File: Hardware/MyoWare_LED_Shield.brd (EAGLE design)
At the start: 52.1 x 21.6 mm, 20 parts, among them IC1 LM3914V

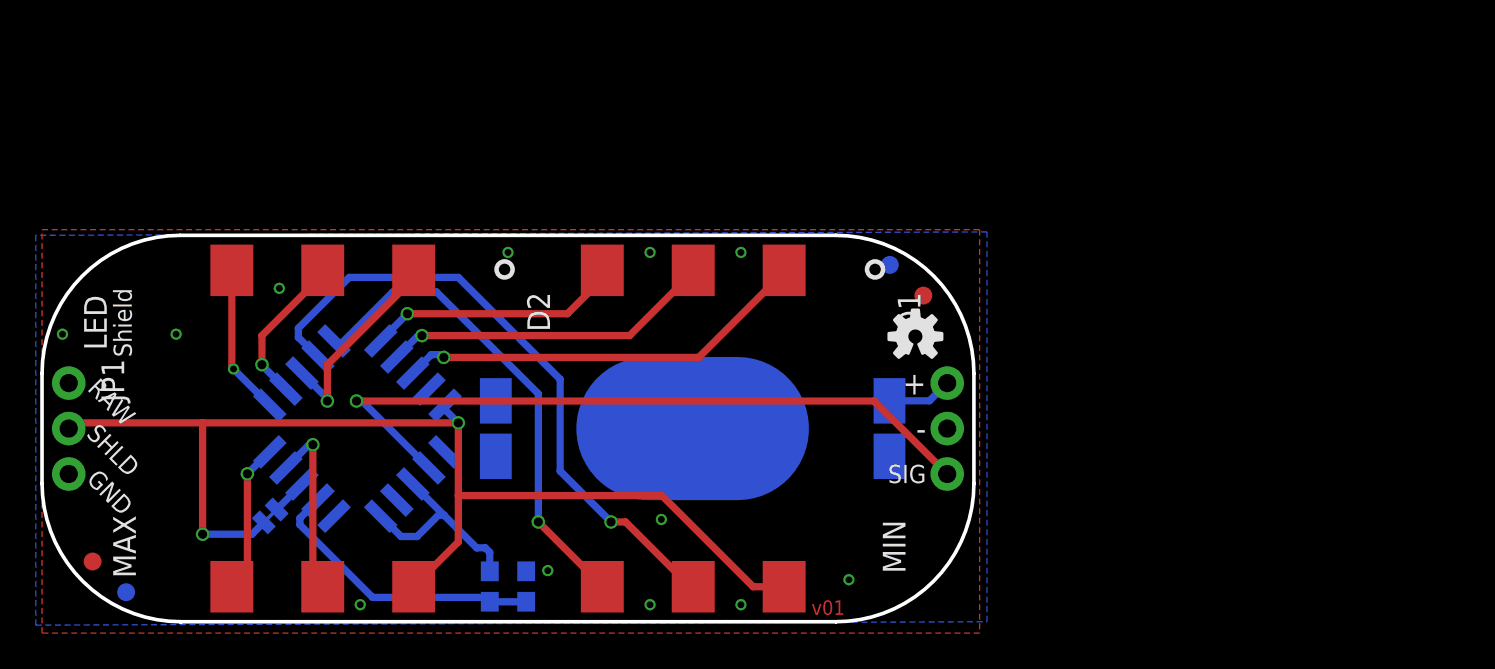
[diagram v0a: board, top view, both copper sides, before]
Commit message: Started move to LiPo based design
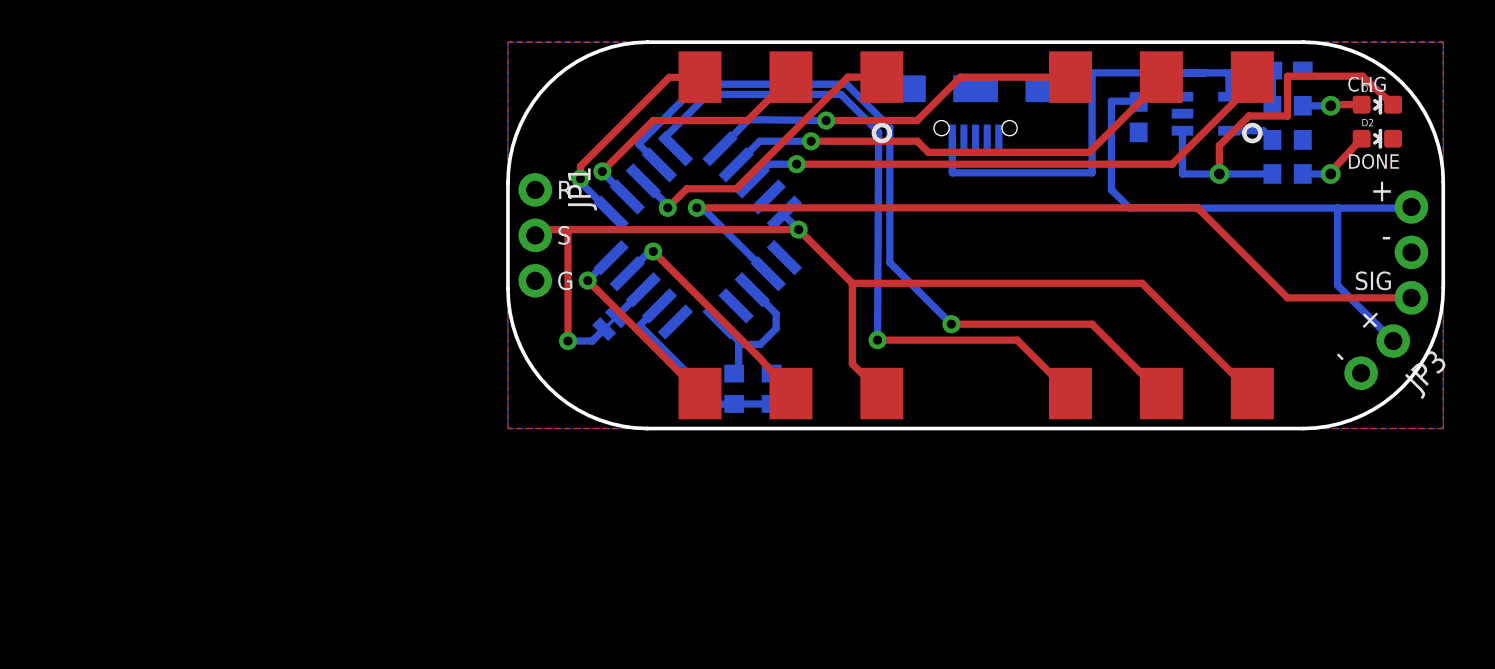
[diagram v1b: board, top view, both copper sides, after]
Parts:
- removed BAT1: 20mm coincell, SparkFun-Electromechanical:BATTCON_20MM_4LEGS
- removed FID1, FID2, FID3, FID4: FIDUCIAL1X2, SparkFun-Aesthetics:FIDUCIAL-1X2
- removed LOGO1: SFE_LOGO_NAME_FLAME.1_INCH, SparkFun-Aesthetics:SFE_LOGO_NAME_FLAME_.1
- removed LOGO2: OSHW-LOGOS, SparkFun-Aesthetics:OSHW-LOGO-S
- removed U$3: (no value), advancer-technologies:ROHS
- removed U$5: (no value), advancer-technologies:PB-FREE
- added C1, C2: 4.7uF, SparkFun-Capacitors:0603-CAP
- added JP3: (no value), SparkFun-Connectors:1X02_NO_SILK
- added JP4: (no value), SparkFun-Connectors:USB-B-MICRO-SMD_V03
- added R3, R5: 330, resistor:R0603
- added R4: 10k, resistor:R0603
- added U$1, U$2: SMA-B500, advancer-technologies:LED_BAR_SMD
- added U1: MCP73831, SparkFun-PowerIC:SOT23-5
- D1, D2: value SMA-B500 -> RED; device Testing:LED_BAR_SMD -> SparkFun-LED:LED-0603
- IC1: device Testing:PLCC20S -> national-semiconductor:PLCC20S
- R1: value 10K -> 6.49k; device SparkFun-Resistors:0603-RES -> resistor:R0603
- R2: value 8K2 -> 7.5k; device SparkFun-Resistors:0603-RES -> resistor:R0603
- SJ1: value JUMPER-PAD-2-NC_BY_TRACE -> SOLDERJUMPERTRACE; device SparkFun-Passives:PAD-JUMPER-2-NC_BY_TRACE_YES_SILK -> SparkFun:SJ_2S-TRACE
- moved D2 61.1 mm to (48.6, 16.2), turned to 270 degrees
- moved D1 42.3 mm to (48.6, 18.1), turned to 270 degrees
- moved U$6 34.0 mm to (26.1, 2.22)
- moved JP1 28.2 mm to (1.52, 13.3)
- moved JP2 27.7 mm to (50.5, 12.4)
- moved FRAME1 27.7 mm to (-12.2, -11.7)
- moved U$9 24.3 mm to (4.89, 17.6)
- moved IC1 21.9 mm to (10.6, 10.8)
- moved SJ1 21.9 mm to (5.73, 5.91)
- moved R2 17.6 mm to (14.7, 2.22)
- moved R1 17.6 mm to (12.6, 2.22)
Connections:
- removed net VCC: BAT1.1, JP2.1
- new net +VS: C2.1, JP2.1, JP3.1, U1.3
- new net N$10: D1.A, R3.1
- new net N$15: D1.C, R5.1, U1.1
- new net N$17: R4.2, U1.5
- new net N$7: C1.1, JP4.VBUS1, R3.2, U1.4
- new net N$9: D2.A, R5.2
- net GND: now also C1.2, C2.2, D2.C, JP3.2, JP4.GND1, R4.1, U1.2; no longer BAT1.2
- net N$1: now also U$1.1; no longer D1.1
- net N$11: now also U$2.2; no longer D2.2
- net N$12: now also U$2.3; no longer D2.3
- net N$13: now also U$2.4; no longer D2.4
- net N$14: now also U$2.5; no longer D2.5
- net N$2: now also U$1.2; no longer D1.2
- net N$3: now also U$1.5; no longer D1.5
- net N$4: now also U$1.3; no longer D1.3
- net N$5: now also U$2.1; no longer D2.1
- net N$8: now also U$1.4; no longer D1.4
- net SHLD_PWR: now also U$1.6, U$2.6; no longer D1.6, D2.6
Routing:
- net +VS: track 0.00 -> 35.2 mm
- net N$7: track 0.00 -> 30.1 mm
- net N$15: track 0.00 -> 22.3 mm, vias 0 -> 1
- net N$8: track 27.3 -> 38.3 mm
- net N$3: track 35.7 -> 44.1 mm
- net N$2: track 18.6 -> 26.4 mm
- net N$1: track 23.3 -> 30.6 mm
- net SIG: track 40.3 -> 47.5 mm
- net N$4: track 14.3 -> 21.3 mm
- net N$11: track 8.60 -> 14.7 mm
- net N$5: track 11.5 -> 17.1 mm
- net N$19: track 16.2 -> 10.7 mm
- net N$9: track 0.00 -> 4.21 mm, vias 0 -> 1
- net VCC: track 3.63 -> 0.00 mm
- net N$12: track 8.55 -> 12.1 mm
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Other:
- board size 52.1 x 21.6 mm -> 52.3 x 21.6 mm
- board text added: "BATTERY GOES HERE"
- board text added: "CHG"
- board text added: "DONE"
- board text added: "G"
- board text added: "R"
- board text added: "S"
- board text removed: "All units in inches"
- board text removed: "GND"
- board text removed: "LED"
- board text removed: "MAX"
- board text removed: "MIN"
- board text removed: "RAW"
- board text removed: "SHLD"
- board text removed: "Shield"
- board text removed: "v01"

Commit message: Design rules checked
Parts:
- removed IC1: LM3914V, national-semiconductor:PLCC20S
- removed SJ1: SOLDERJUMPERTRACE, SparkFun:SJ_2S-TRACE
- removed U$1, U$2: SMA-B500, advancer-technologies:LED_BAR_SMD
- added D3, D4: SMA-B500, Testing:LED_BAR_SMD
- added FID1, FID2, FID3, FID4: FIDUCIAL1X2, SparkFun-Aesthetics:FIDUCIAL-1X2
- added LOGO1: SFE_LOGO_FLAME.1_INCH, SparkFun-Aesthetics:SFE_LOGO_FLAME_.1
- added LOGO2: OSHW-LOGOS, SparkFun-Aesthetics:OSHW-LOGO-S
- added MODE: JUMPER-PAD-2-NC_BY_TRACE, SparkFun-Passives:PAD-JUMPER-2-NC_BY_TRACE_YES_SILK
- added U2: LM3914V, Testing:PLCC20S
- JP2: value Power -> Signal
- JP3: value (none) -> LiPo
- R3, R5: device resistor:R0603 -> SparkFun-Resistors:0603-RES
- R4: value 10k -> 10K; device resistor:R0603 -> SparkFun-Resistors:0603-RES
- moved JP2 1.08 mm to (50.5, 13.5)
- moved D2 0.13 mm to (48.6, 16.3)
- moved R3 0.13 mm to (43.6, 18.2)
- moved R5 0.13 mm to (43.6, 14.4)
- moved JP3 0.13 mm to (49.5, 5.02)
- moved R1 0.13 mm to (12.6, 2.35)
- moved R2 0.13 mm to (14.7, 2.35)
- moved U$6 0.13 mm to (26.1, 2.35)
- moved C1 0.13 mm to (43.6, 20.1)
- moved C2 0.13 mm to (35.2, 17.5)
- moved D1 0.13 mm to (48.6, 18.2)
- moved JP1 0.13 mm to (1.52, 13.5)
- moved JP4 0.13 mm to (26.1, 19.1)
- moved R4 0.13 mm to (43.6, 16.3)
- moved U$9 0.13 mm to (4.89, 17.7)
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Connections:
- net N$7 renamed VBUS
- net GND: now also U2.2, U2.4; no longer IC1.2, IC1.4
- net N$1: now also D3.1, U2.1; no longer IC1.1, U$1.1
- net N$11: now also D4.2, U2.15; no longer IC1.15, U$2.2
- net N$12: now also D4.3, U2.14; no longer IC1.14, U$2.3
- net N$13: now also D4.4, U2.13; no longer IC1.13, U$2.4
- net N$14: now also D4.5, U2.12; no longer IC1.12, U$2.5
- net N$19: now also U2.10; no longer IC1.10
- net N$2: now also D3.2, U2.20; no longer IC1.20, U$1.2
- net N$20: now also U2.6, U2.8; no longer IC1.6, IC1.8
- net N$3: now also D3.5, U2.17; no longer IC1.17, U$1.5
- net N$4: now also D3.3, U2.19; no longer IC1.19, U$1.3
- net N$5: now also D4.1, U2.16; no longer IC1.16, U$2.1
- net N$6: now also MODE.1, U2.11; no longer IC1.11, SJ1.1
- net N$8: now also D3.4, U2.18; no longer IC1.18, U$1.4
- net SHLD_PWR: now also D3.6, D4.6, MODE.2, U2.3; no longer IC1.3, SJ1.2, U$1.6, U$2.6
- net SIG: now also U2.5; no longer IC1.5
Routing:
- net +VS: track 35.2 -> 36.1 mm
- net N$3: track 44.1 -> 43.6 mm
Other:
- board size 52.3 x 21.6 mm -> 52.3 x 21.8 mm
- board text added: "ALL UNITS IN INCHES"
- board text added: "LED SHIELD"
- board text added: "MODE"
- board text added: "v02"

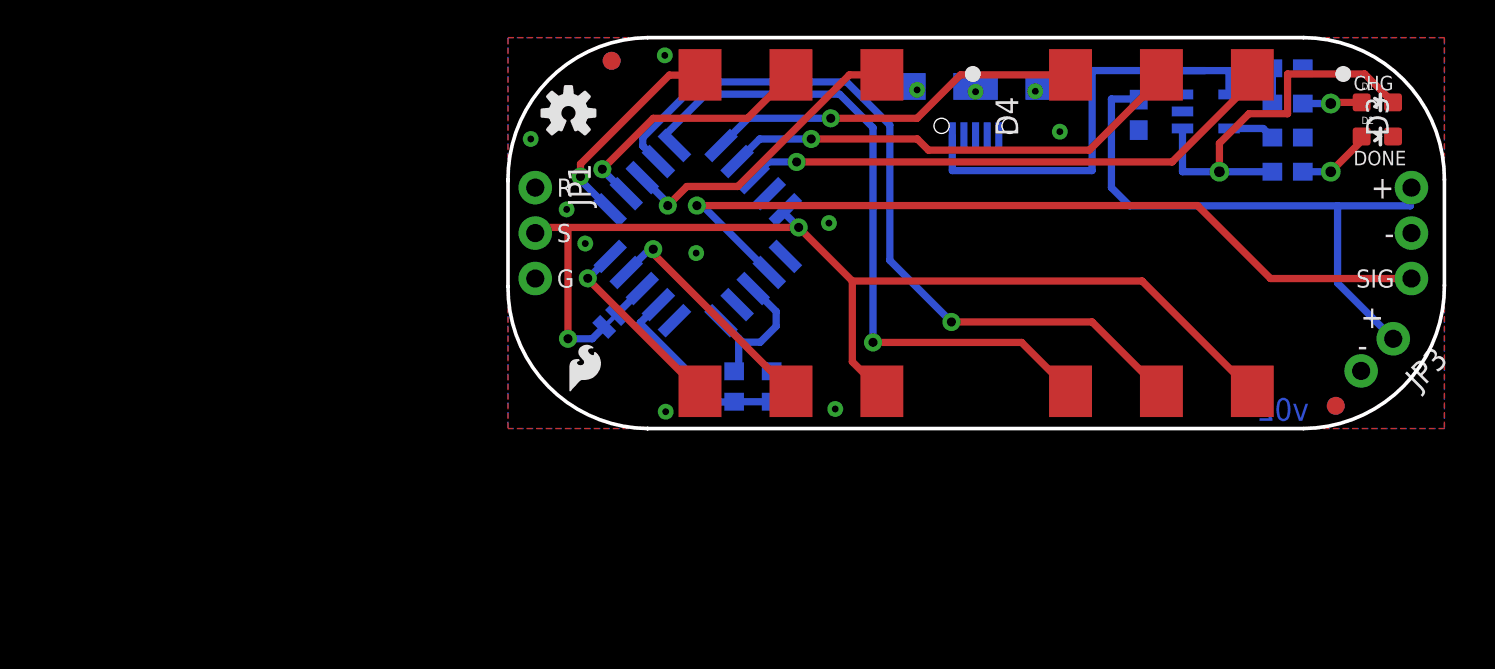
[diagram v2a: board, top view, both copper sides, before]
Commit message: Tweaks (mostly silk and info)
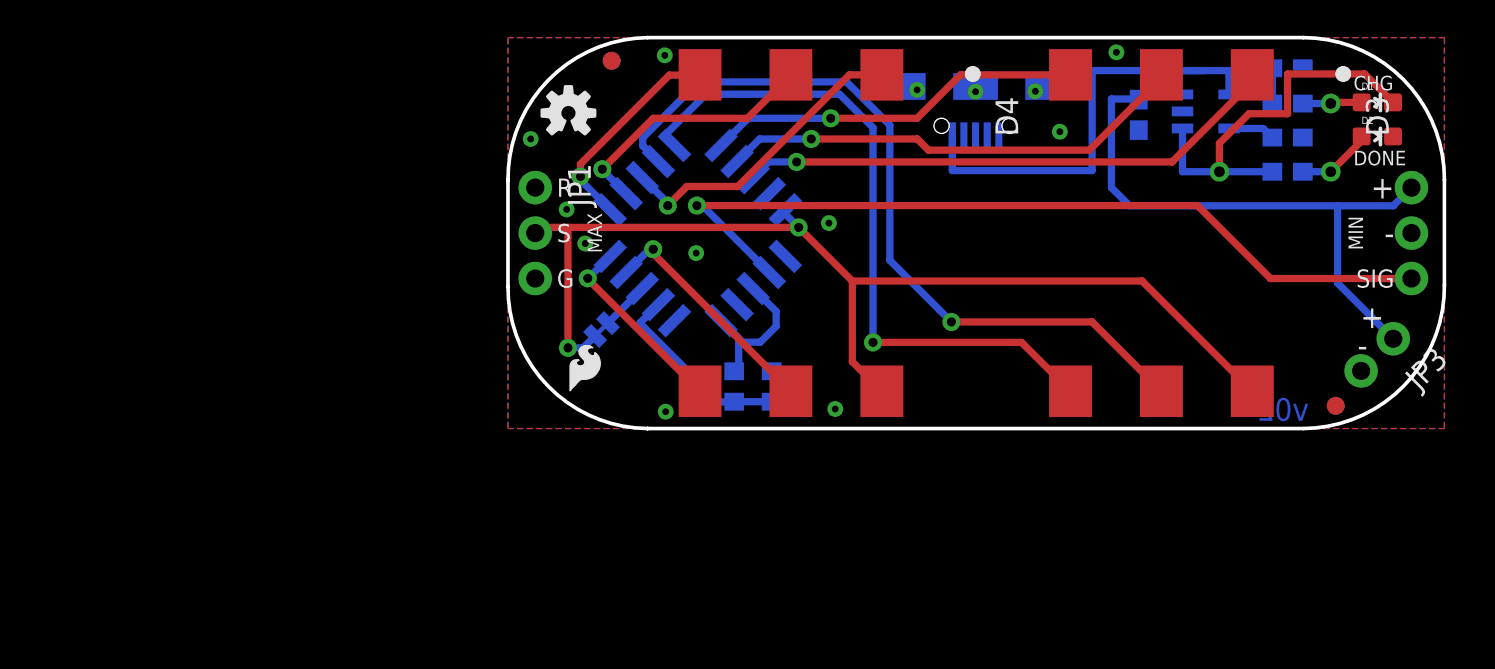
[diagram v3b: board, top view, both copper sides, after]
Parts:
- moved MODE 0.72 mm to (5.23, 5.53)
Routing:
- net N$6: track 2.01 -> 2.73 mm
- net +VS: track 36.1 -> 35.6 mm
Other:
- board text added: "MAX"
- board text added: "MIN"
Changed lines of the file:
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@@
 <setting verticaltext="up"/>
 </settings>
-<grid distance="0.01" unitdist="inch" unit="inch" style="lines" multiple="1" display="yes" altdistance="1.96850394" altunitdist="mil" altunit="mil"/>
+<grid distance="0.02" unitdist="inch" unit="inch" style="lines" multiple="1" display="yes" altdistance="1.96850394" altunitdist="mil" altunit="mil"/>
 <layers>
 <layer number="1" name="Top" color="4" fill="1" visible="yes" active="yes"/>
@@
 <text x="48.70835" y="5.774646875" size="1.27" layer="22" ratio="20" rot="R135" align="center-left">+</text>
 <text x="46.82195" y="4.041546875" size="1.27" layer="22" ratio="17" rot="R135" align="center-left">-</text>
-<text x="47.244" y="19.304" size="0.8128" layer="21" ratio="17" align="center-left">CHG</text>
-<text x="47.244" y="15.113" size="0.8128" layer="21" ratio="17" align="center-left">DONE</text>
+<text x="47.244" y="19.304" size="0.8128" layer="21" font="vector" ratio="17" align="center-left">CHG</text>
+<text x="47.244" y="15.113" size="0.8128" layer="21" font="vector" ratio="17" align="center-left">DONE</text>
 <text x="18.288" y="-11.684" size="1.778" layer="51" font="vector">Brian E Kaminski of Advancer Technologies</text>
 <text x="-0.762" y="-14.478" size="1.778" layer="51" font="vector">Revised by: Brent Wilkins</text>
@@
 <text x="49.38" y="8.382" size="1.016" layer="22" ratio="17" rot="MR180" align="center-right">SIG</text>
 <text x="49.276" y="10.922" size="1.27" layer="22" ratio="17" rot="MR180" align="center-right">-</text>
-<text x="4.98475" y="3.6322" size="1.27" layer="22" font="vector" ratio="15" rot="MR180" align="center">MODE</text>
+<text x="5.49275" y="2.6162" size="1.27" layer="22" font="vector" ratio="15" rot="MR180" align="center">MODE</text>
 <text x="26.5176" y="22.9108" size="1.016" layer="47" font="vector" ratio="17" align="bottom-center">ALL UNITS IN INCHES</text>
 <text x="15.5956" y="20.2946" size="0.8128" layer="22" font="vector" ratio="17" rot="MR0" align="bottom-center">LED SHIELD</text>
 <dimension x1="0" y1="7.9375" x2="52.324" y2="8.001" x3="26.162" y3="-2.266596875" textsize="1.016" textratio="17" layer="47" dtype="horizontal" unit="inch"/>
 <dimension x1="7.8105" y1="0" x2="7.8105" y2="21.844" x3="-1.6764" y3="10.922" textsize="1.016" textratio="17" layer="47" unit="inch"/>
+<text x="4.849" y="10.922" size="0.8128" layer="21" font="vector" ratio="17" rot="R90" align="center">MAX</text>
+<text x="47.371" y="10.922" size="0.8128" layer="21" font="vector" ratio="17" rot="R90" align="center">MIN</text>
 </plain>
 <attributes>
@@
 <element name="U$6" library="advancer-technologies" package="ADVANCER_LOGO" value="" x="26.127" y="2.3495" rot="MR0"/>
 <element name="JP1" library="SparkFun-Connectors" package="1X03_NO_SILK" value="Power" x="1.524" y="13.462" rot="R270"/>
-<element name="MODE" library="SparkFun-Passives" package="PAD-JUMPER-2-NC_BY_TRACE_YES_SILK" value="JUMPER-PAD-2-NC_BY_TRACE" x="5.733596875" y="6.040203125" rot="MR315"/>
+<element name="MODE" library="SparkFun-Passives" package="PAD-JUMPER-2-NC_BY_TRACE_YES_SILK" value="JUMPER-PAD-2-NC_BY_TRACE" x="5.225596875" y="5.532203125" rot="MR315"/>
 <element name="JP4" library="SparkFun-Connectors" package="USB-B-MICRO-SMD_V03" value="" x="26.127" y="19.1135" rot="MR270">
 <attribute name="PROD_ID" value="CONN-11752" x="26.127" y="19.1135" size="1.778" layer="28" font="vector" ratio="15" rot="MR270" display="off"/>
@@
 <via x="17.9324" y="11.4808" extent="1-16" drill="0.381"/>
 <via x="8.763" y="20.8534" extent="1-16" drill="0.381"/>
+<via x="33.9976" y="21.0222" extent="1-16" drill="0.381"/>
 </signal>
 <signal name="SIG">
@@
 <wire x1="49.4665" y1="5.0165" x2="46.355" y2="8.128" width="0.4064" layer="16"/>
 <wire x1="46.355" y1="8.128" x2="46.355" y2="12.446" width="0.4064" layer="16"/>
-<wire x1="46.355" y1="12.446" x2="50.419" y2="12.446" width="0.4064" layer="16"/>
-<wire x1="50.419" y1="12.446" x2="50.4825" y2="13.462" width="0.4064" layer="16"/>
+<wire x1="46.355" y1="12.446" x2="49.4665" y2="12.446" width="0.4064" layer="16"/>
+<wire x1="49.4665" y1="12.446" x2="50.4825" y2="13.462" width="0.4064" layer="16"/>
 </signal>
 <signal name="SHLD_PWR">
@@
 <wire x1="3.3528" y1="11.2395" x2="1.7526" y2="11.2395" width="0.4064" layer="1"/>
 <via x="16.2433" y="11.2395" extent="1-16" drill="0.508"/>
-<via x="3.3528" y="5.0165" extent="1-16" drill="0.508"/>
-<wire x1="5.3743875" y1="5.680990625" x2="4.709896875" y2="5.0165" width="0.4064" layer="16"/>
-<wire x1="4.709896875" y1="5.0165" x2="3.3528" y2="5.0165" width="0.4064" layer="16"/>
-<wire x1="3.3528" y1="11.2395" x2="3.3528" y2="5.0165" width="0.4064" layer="1"/>
+<via x="3.3528" y="4.5085" extent="1-16" drill="0.508"/>
+<wire x1="3.3528" y1="11.2395" x2="3.3528" y2="4.5085" width="0.4064" layer="1"/>
 <wire x1="16.2433" y1="11.2395" x2="19.2405" y2="8.2423" width="0.4064" layer="1"/>
 <wire x1="35.4322" y1="8.2423" x2="19.2405" y2="8.2423" width="0.4064" layer="1"/>
@@
 <wire x1="15.4305" y1="12.0523" x2="15.4305" y2="12.155896875" width="0.4064" layer="16"/>
 <wire x1="15.4305" y1="12.155896875" x2="15.499446875" y2="12.22484375" width="0.4064" layer="16"/>
+<wire x1="3.3528" y1="4.5085" x2="4.201896875" y2="4.5085" width="0.4064" layer="16"/>
+<wire x1="4.201896875" y1="4.5085" x2="4.8663875" y2="5.172990625" width="0.4064" layer="16"/>
 </signal>
 <signal name="RAW">
@@
 <contactref element="U2" pad="11"/>
 <contactref element="MODE" pad="1"/>
-<wire x1="6.092809375" y1="6.3994125" x2="6.092809375" y2="6.41030625" width="0.4064" layer="16"/>
-<wire x1="6.092809375" y1="6.41030625" x2="7.50560625" y2="7.823103125" width="0.4064" layer="16"/>
+<wire x1="7.50560625" y1="7.823103125" x2="7.50560625" y2="7.812209375" width="0.4064" layer="16"/>
+<wire x1="7.50560625" y1="7.812209375" x2="5.584809375" y2="5.8914125" width="0.4064" layer="16"/>
 </signal>
 <signal name="VBUS">

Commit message: Moved the USB jack to board edge to prevent interference with part flair
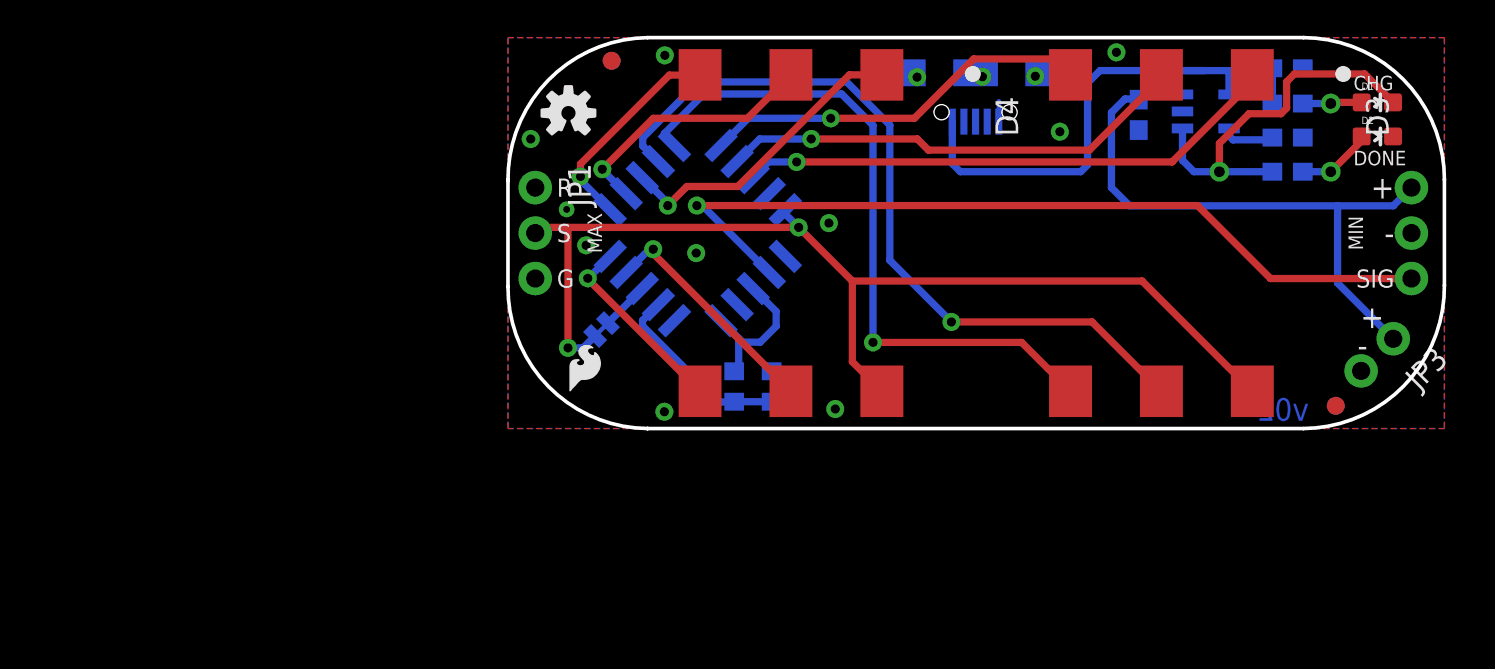
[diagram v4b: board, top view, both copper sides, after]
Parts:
- moved JP4 0.76 mm to (26.1, 19.9)
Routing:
- net N$4: track 21.2 -> 22.2 mm
- net N$8: track 38.3 -> 39.3 mm
- net GND: track 0.00 -> 0.84 mm
- net N$15: track 22.3 -> 21.5 mm
